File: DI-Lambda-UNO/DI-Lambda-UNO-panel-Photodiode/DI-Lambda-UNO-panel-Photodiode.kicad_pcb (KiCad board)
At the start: 2 copper layers, 33.2 x 26.6 mm, 8 parts, among them J1 Conn_01X06, U1 TP1271, U2 MCP3421A0T-E/CH

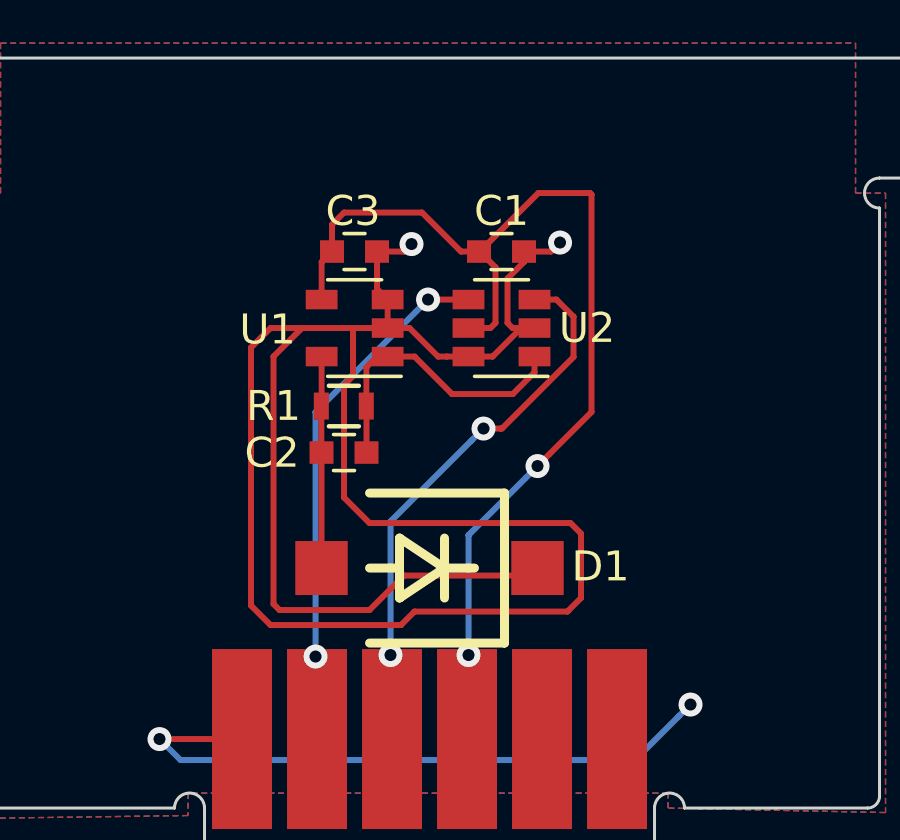
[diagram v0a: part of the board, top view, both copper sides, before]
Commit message: Photodiode board: Fix the op amp pinout
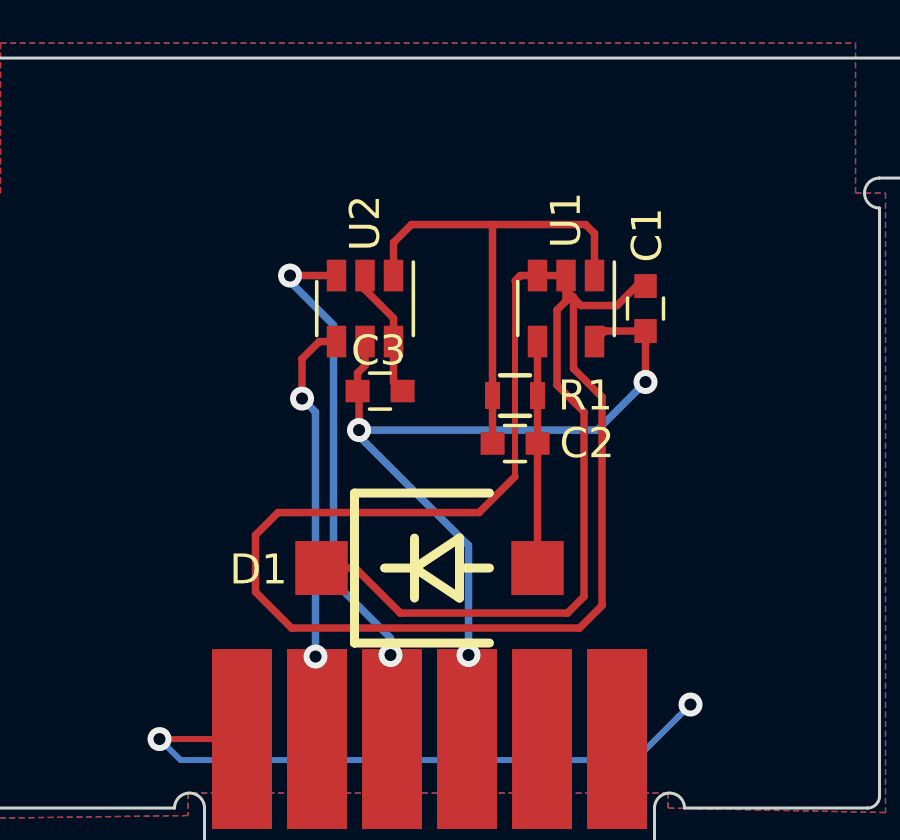
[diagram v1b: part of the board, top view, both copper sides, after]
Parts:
- moved U1 7.08 mm to (164.6, 75.3), turned to 270 degrees
- moved R1 5.72 mm to (162.8, 78.2), turned to 0 degrees
- moved C2 5.71 mm to (162.8, 79.8), turned to 0 degrees
- moved C1 5.16 mm to (167.2, 75.3), turned to 90 degrees
- moved C3 4.73 mm to (158.3, 78.1)
- moved U2 4.60 mm to (157.8, 75.3), turned to 270 degrees
- turned D1 to 180 degrees
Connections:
- U1 pad 4: /VCC -> Net-(C2-Pad2)
- U1 pad 5: Net-(C2-Pad2) -> /VCC
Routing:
- net /VCC: track 33.4 -> 25.8 mm, vias 2 -> 3
- net Net-(C2-Pad1): track 9.94 -> 16.9 mm
- net /SDA: track 15.6 -> 12.3 mm
- net GND: track 96.5 -> 93.5 mm, vias 4 -> 2
- net Net-(C2-Pad2): track 7.06 -> 7.60 mm

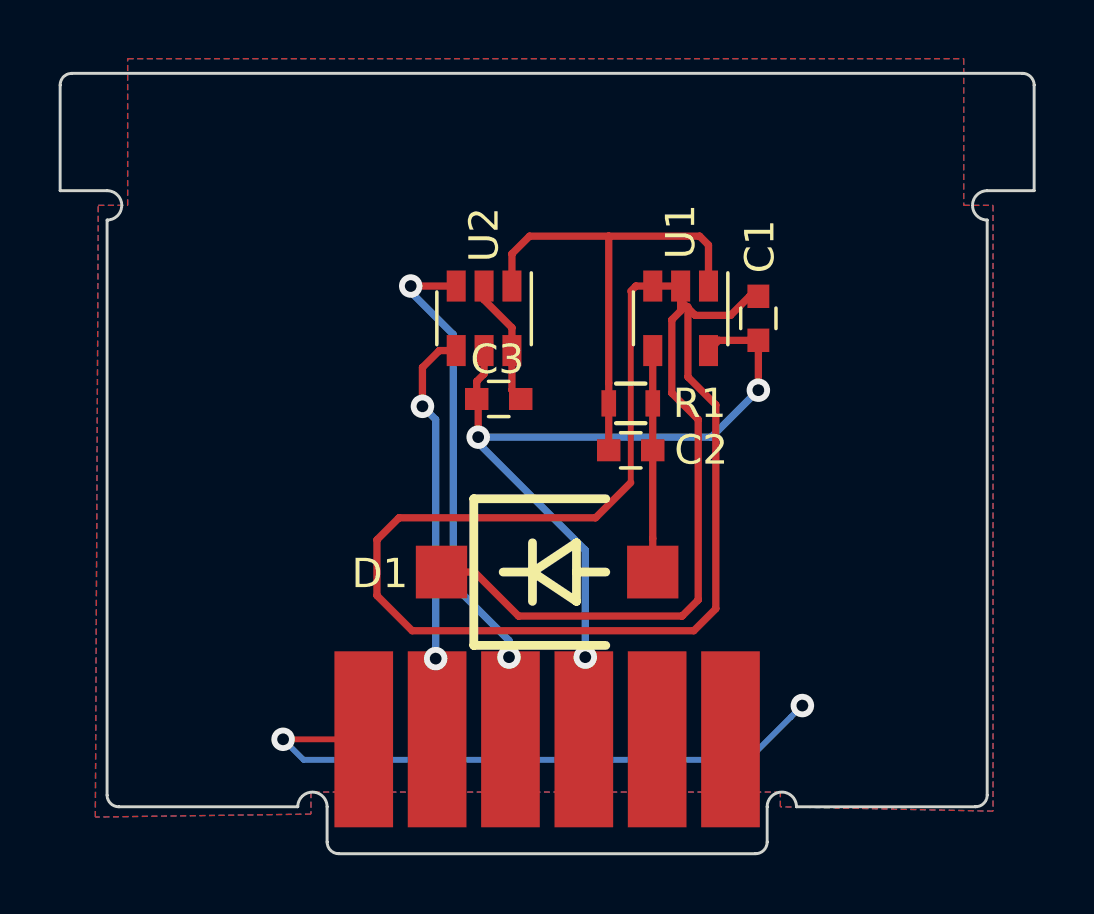
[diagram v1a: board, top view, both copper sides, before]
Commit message: Photodiode board: Convert to 18mm height
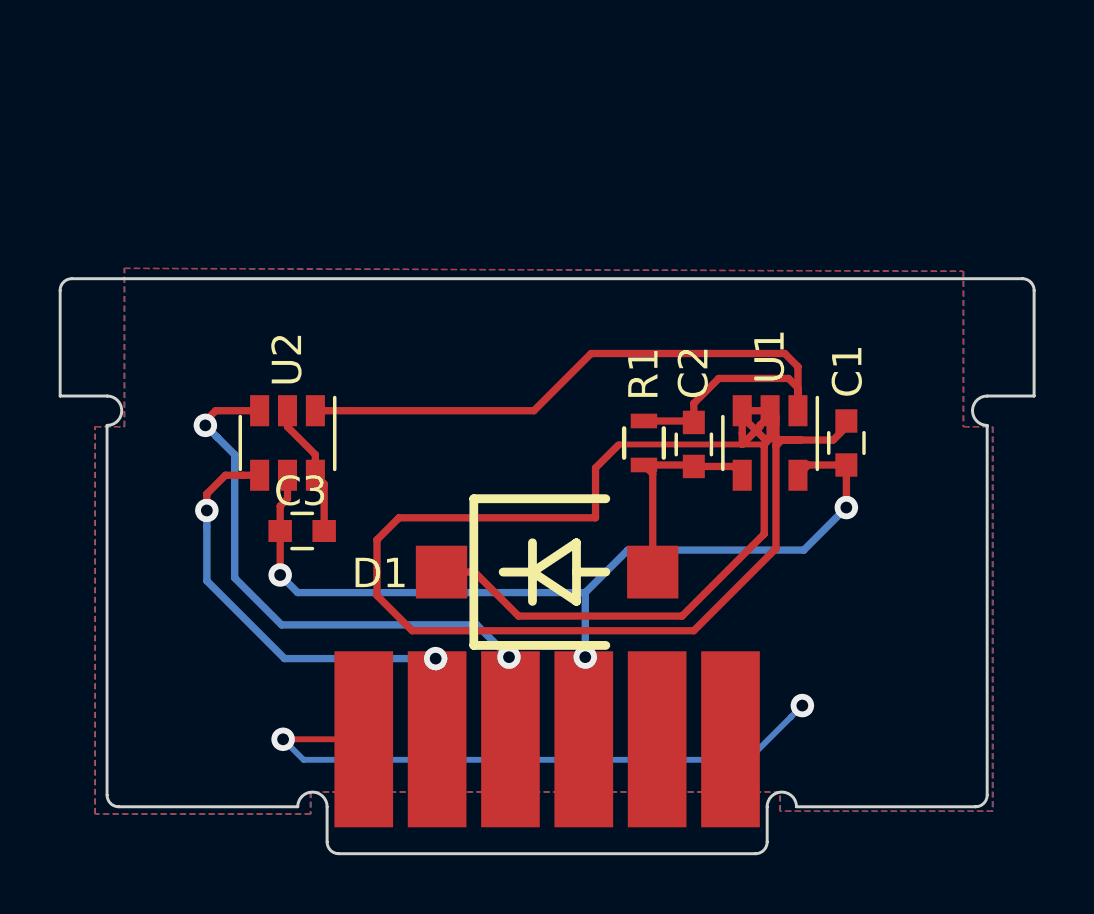
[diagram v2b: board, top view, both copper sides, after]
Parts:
- moved C3 8.07 mm to (151.7, 82.6)
- moved U2 7.93 mm to (151.2, 79.6)
- moved U1 5.23 mm to (167.6, 79.6)
- moved C1 5.20 mm to (170.2, 79.6)
- moved C2 2.16 mm to (165.0, 79.7), turned to 270 degrees
- moved R1 1.42 mm to (163.3, 79.6), turned to 270 degrees
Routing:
- net Net-(C2-Pad1): track 16.9 -> 26.1 mm
- net GND: track 93.5 -> 89.5 mm
- net /VCC: track 25.8 -> 29.7 mm
- net /SCL: track 16.4 -> 19.0 mm
- net /SDA: track 12.3 -> 14.7 mm
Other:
- board size 33.2 x 26.6 mm -> 33.2 x 19.6 mm
- board text added: "DI-Lambda UNO v1.3"
- board text removed: "DI-Lambda UNO v1.2"

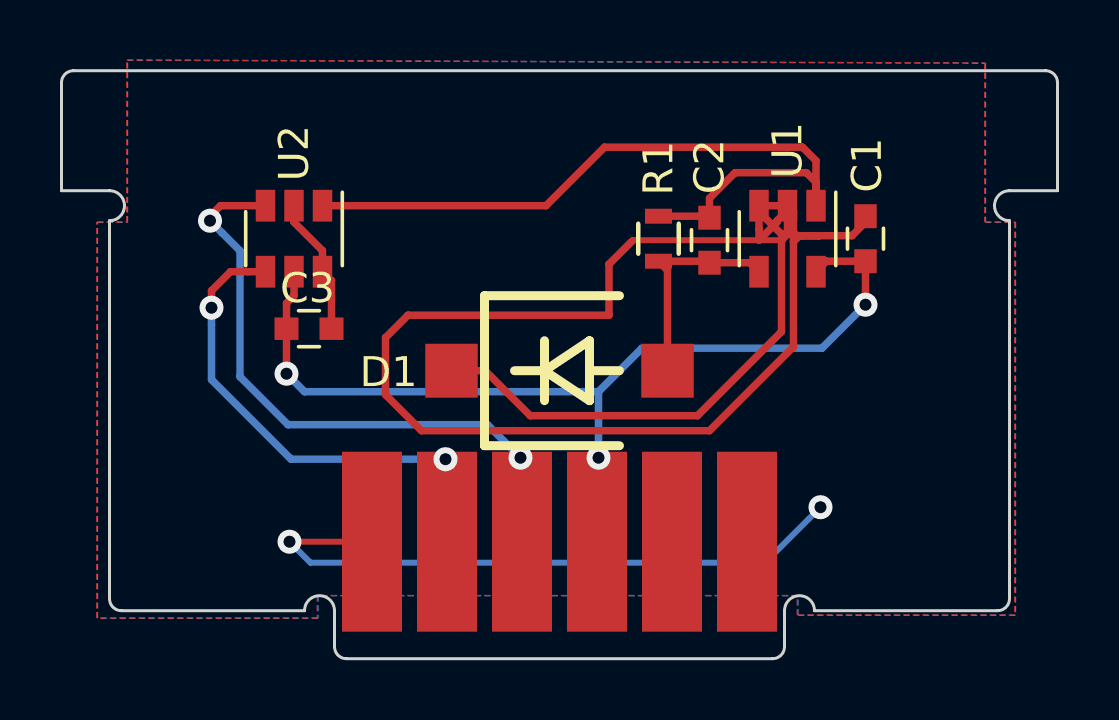
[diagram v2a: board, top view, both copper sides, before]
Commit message: Update schematics to version 1.3
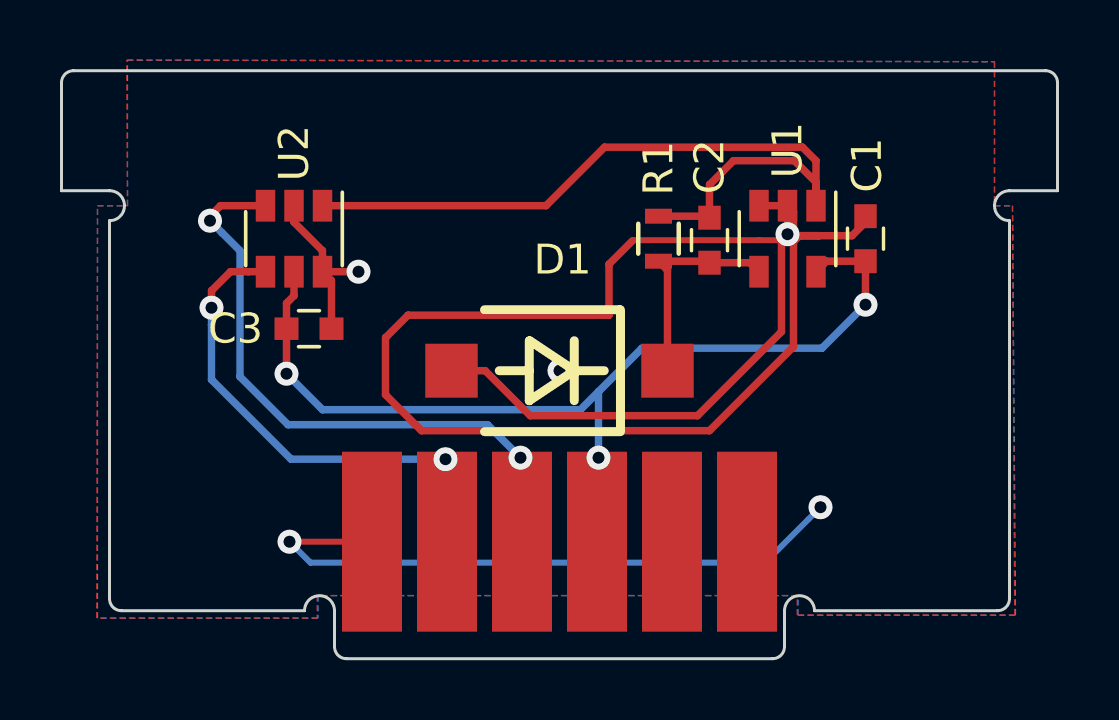
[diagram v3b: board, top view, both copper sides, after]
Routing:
- net GND: track 89.5 -> 86.9 mm, vias 2 -> 5
- net Net-(C2-Pad1): track 26.1 -> 26.7 mm

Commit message: Version 1.5
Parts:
- added MK1: Mounting_Hole, DI-Lambda-module-tabs:Tab_SENSOR, F.Cu at (160.0, 92.0)
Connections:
- J1 pad 1: GND -> /VCC
- J1 pad 4: /VCC -> GND
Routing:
- net GND: track 86.9 -> 68.4 mm, vias 5 -> 3
- net /VCC: track 30.2 -> 34.8 mm, vias 3 -> 2
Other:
- board size 33.2 x 19.6 mm -> 33.2 x 25 mm
- board text added: "DI-Lambda UNO v1.5"
- board text removed: "DI-Lambda UNO v1.3"

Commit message: More missing fotprints
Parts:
- removed C1, C3: 0.1uF 25v, Capacitors_SMD:C_0603
- removed C2: 10pf, Capacitors_SMD:C_0603
- removed R1: 1M, Resistors_SMD:R_0603
- removed U1: TP1271, TO_SOT_Packages_SMD:SOT-23-5
- removed U2: MCP3421A0T-E/CH, TO_SOT_Packages_SMD:SOT-23-6
- added C501: 10pf, Capacitor_SMD:C_0603_1608Metric, F.Cu at (21.6, 12.7)
- added C502: 0.1uF 25v, Capacitor_SMD:C_0603_1608Metric, F.Cu at (8.25, 15.6)
- added C503: 0.1uF 25v, Capacitor_SMD:C_0603_1608Metric, F.Cu at (26.8, 12.6)
- added R501: 1M, Resistor_SMD:R_0603_1608Metric, F.Cu at (19.9, 12.6)
- added U501: TP1271, Package_TO_SOT_SMD:SOT-23-5, F.Cu at (24.2, 12.6)
- added U502: MCP3421A0T-E/CH, Package_TO_SOT_SMD:SOT-23-6, F.Cu at (7.75, 12.6)
- moved D501 158.3 mm to (16.6, 17.0)
- moved J501 158.3 mm to (16.6, 23.7)
- moved MK501 158.3 mm to (16.6, 25.0)
- renumbered D1 to D501, J1 to J501, MK1 to MK501
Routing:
- net Net-(C2-Pad1): track 26.7 -> 0.00 mm
- net Net-(C501-Pad1): track 0.00 -> 26.7 mm
- net (no net): vias 0 -> 1
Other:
- board text added: "DI-Lambda UNO v1.7"
- board text removed: "DI-Lambda UNO v1.5"
